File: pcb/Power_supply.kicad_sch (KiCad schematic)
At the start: 32 parts, among them Q1 Si4368DY, SW1 POWER, U1 LTC3872, U2 TLV1117-33

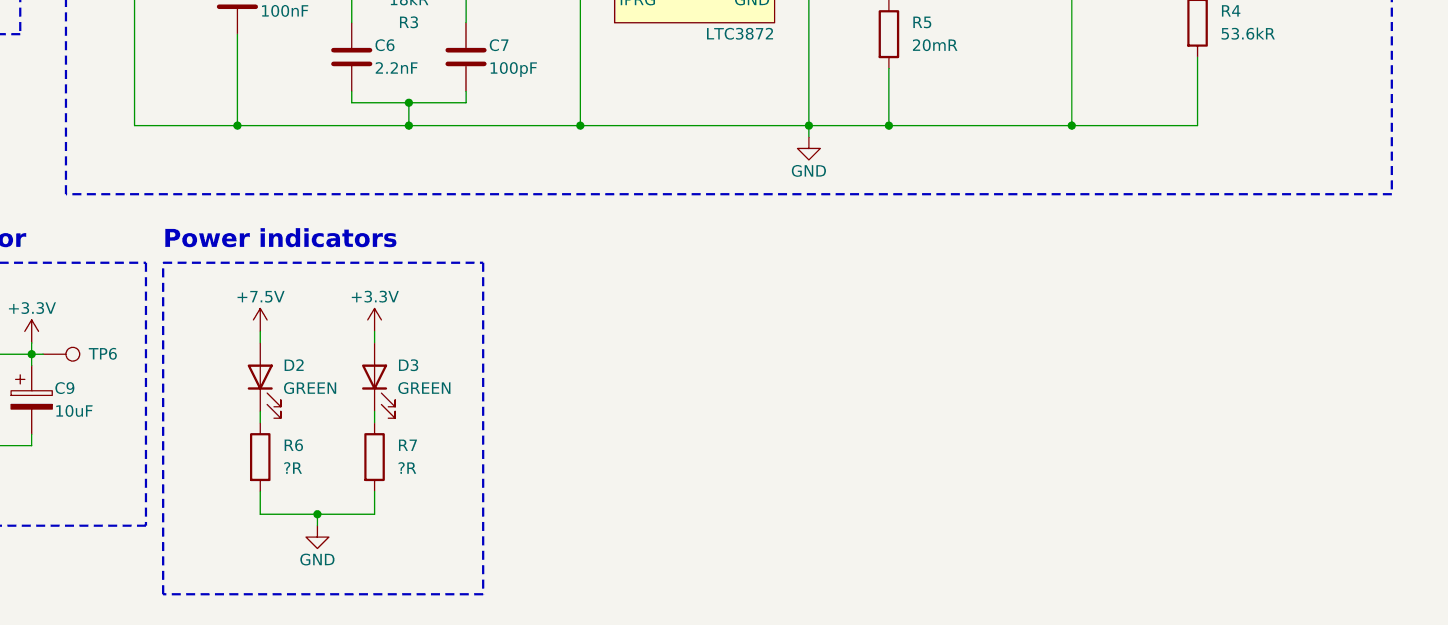
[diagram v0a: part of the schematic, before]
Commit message: [pcb] 4 layer PCB
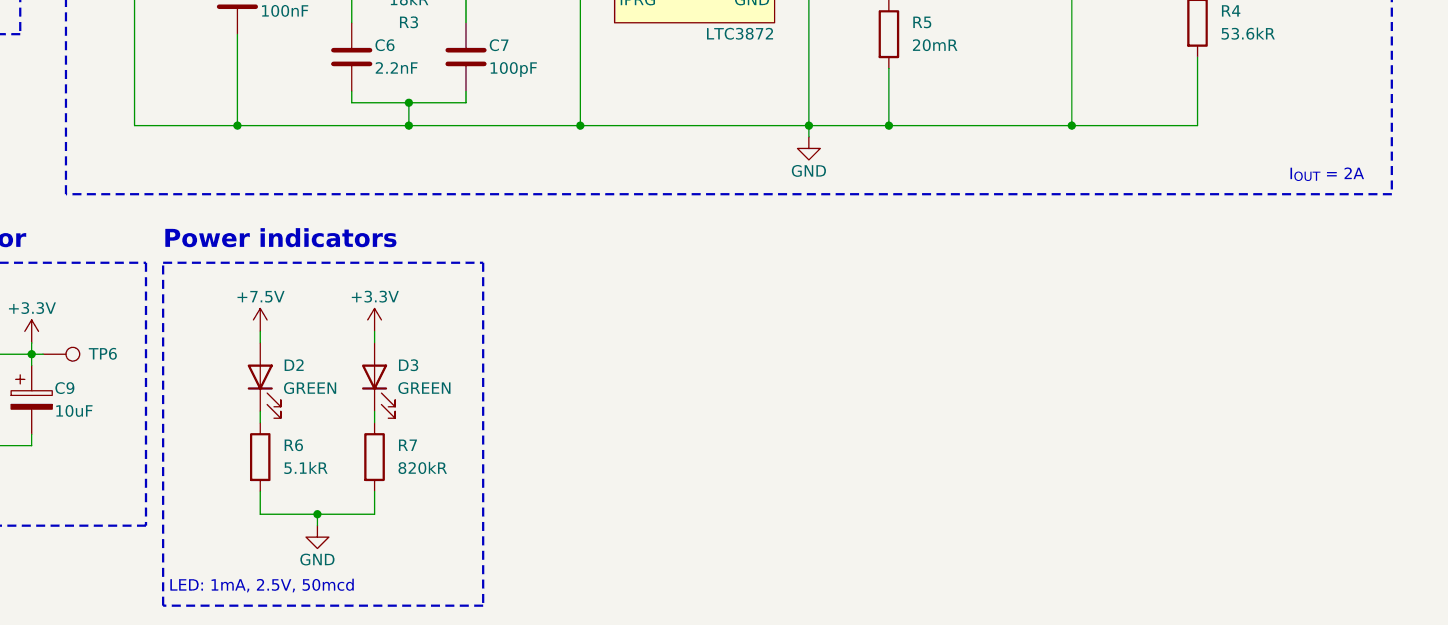
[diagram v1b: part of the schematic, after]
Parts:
- R6: value ?R -> 5.1kR
- R7: value ?R -> 820kR
- U2: footprint Package_TO_SOT_SMD:SOT-223-3_TabPin2 -> Package_TO_SOT_SMD:TO-252-2
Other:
- note added: "I_{OUT} = 2A"
- note added: "LED: 1mA, 2.5V, 50mcd"
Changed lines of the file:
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@@
     (fill (type none))
   )
-  (rectangle (start 71.755 80.01) (end 107.315 116.84)
+  (rectangle (start 71.755 80.01) (end 107.315 118.11)
     (stroke (width 0.25) (type dash))
     (fill (type none))
   )
+  (text "LED: 1mA, 2.5V, 50mcd" (at 72.39 116.84 0)
+    (effects (font (size 1.27 1.27)) (justify left bottom))
+  )
   (text "7.5V boost converter" (at 60.96 21.59 0)
     (effects (font (size 2 2) (thickness 0.4) bold) (justify left bottom))
@@
   (text "3.3V voltage regulator\n" (at 21.59 78.74 0)
     (effects (font (size 2 2) (thickness 0.4) bold) (justify left bottom))
+  )
+  (text "I_{OUT} = 2A" (at 196.85 71.12 0)
+    (effects (font (size 1.27 1.27)) (justify left bottom))
   )
   (symbol (lib_id "Autko:LTC3872") (at 130.81 46.99 0) (unit 1)
@@
       (effects (font (size 1.27 1.27)) (justify left))
     )
-    (property "Value" "?R" (at 97.79 102.87 0)
+    (property "Value" "820kR" (at 97.79 102.87 0)
       (effects (font (size 1.27 1.27)) (justify left))
     )
@@
       (effects (font (size 1.27 1.27)) (justify left))
     )
-    (property "Value" "?R" (at 85.09 102.87 0)
+    (property "Value" "5.1kR" (at 85.09 102.87 0)
       (effects (font (size 1.27 1.27)) (justify left))
     )
@@
       (effects (font (size 1.27 1.27)))
     )
-    (property "Footprint" "Package_TO_SOT_SMD:SOT-223-3_TabPin2" (at 45.72 90.17 0)
-      (effects (font (size 1.27 1.27)) hide)
-    )
+    (property "Footprint" "Package_TO_SOT_SMD:TO-252-2" (at 45.72 90.17 0)
+      (effects (font (size 1.27 1.27)) hide)
+    )

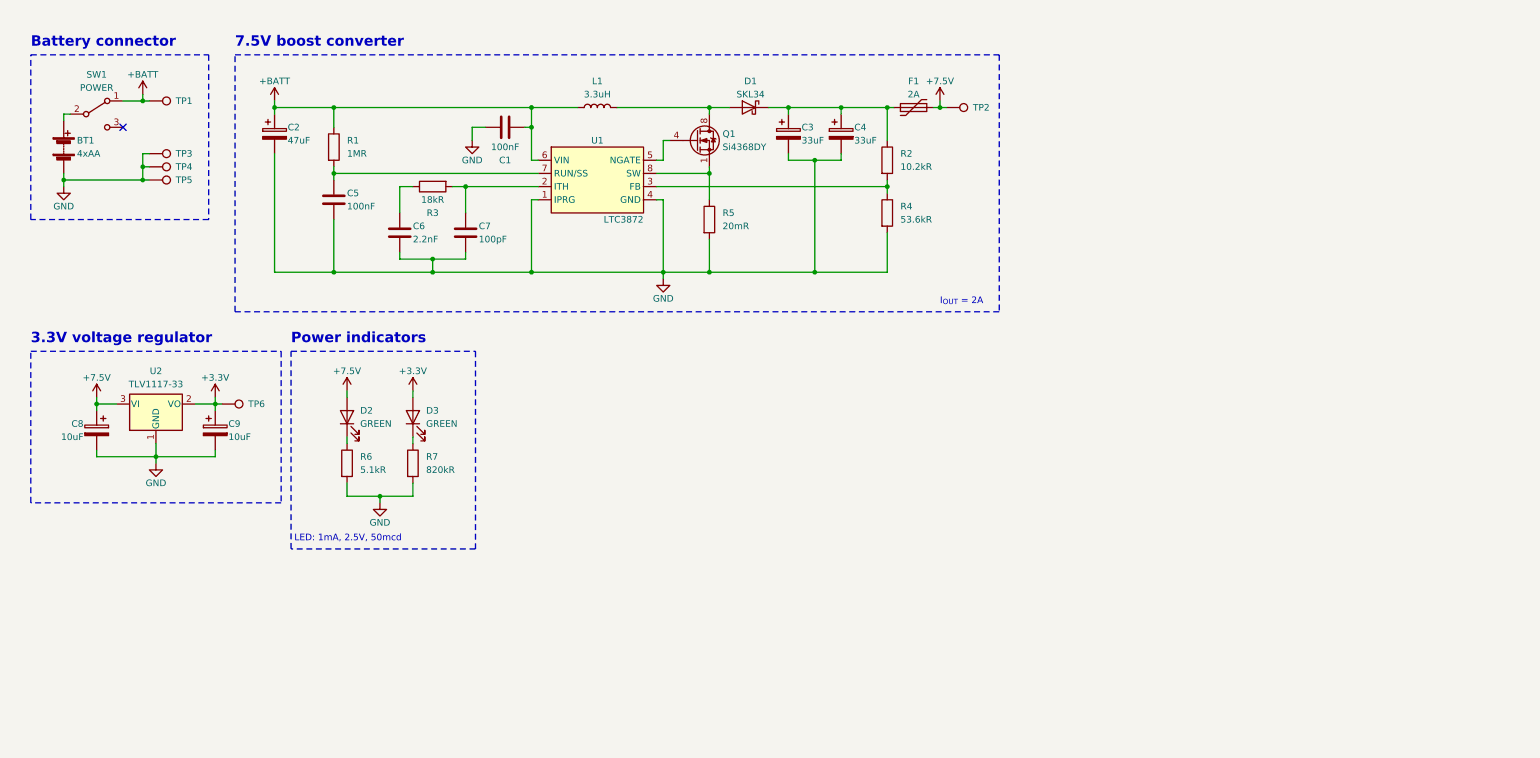
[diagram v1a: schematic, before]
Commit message: [pcb] More final touches, UART test ponts added.
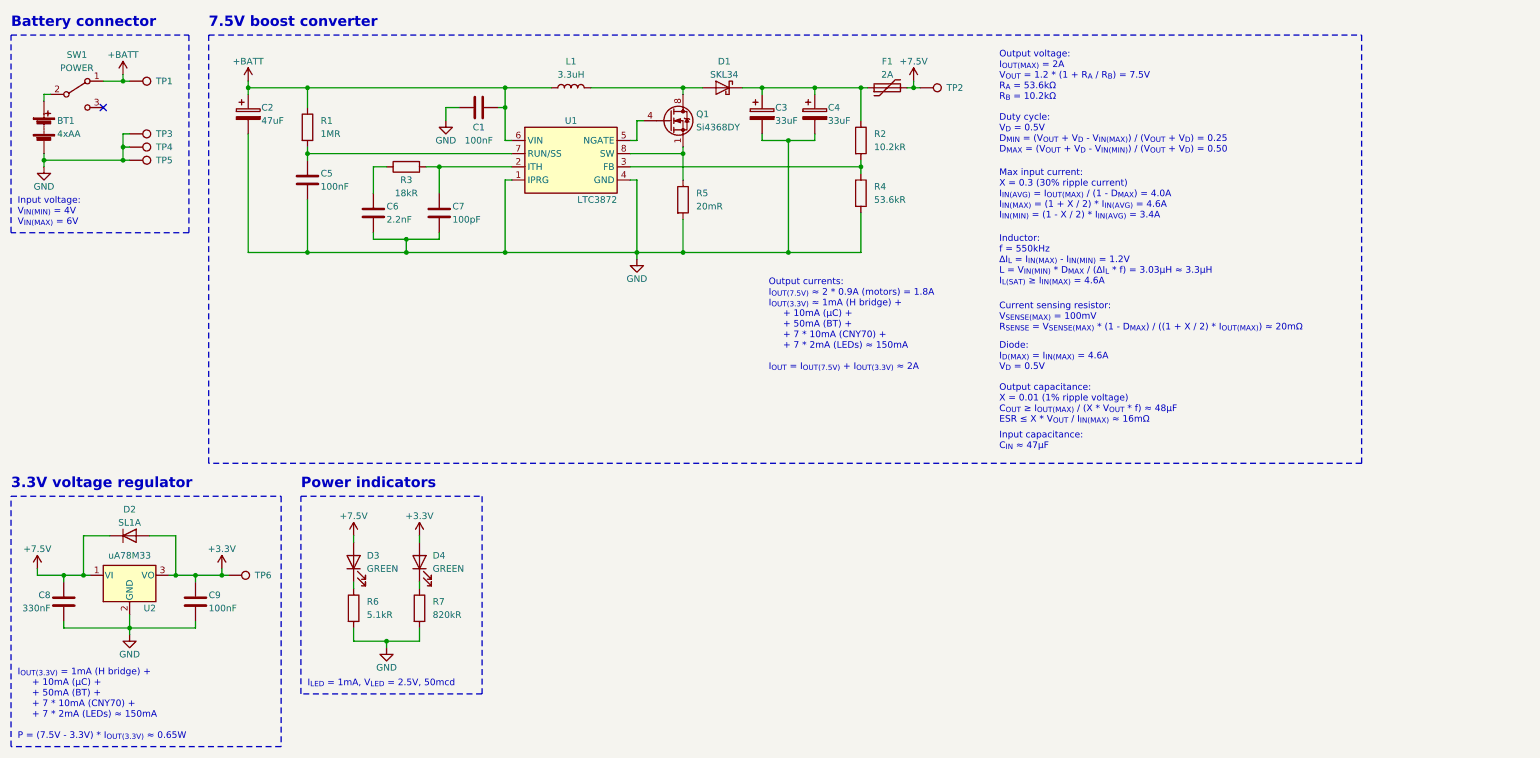
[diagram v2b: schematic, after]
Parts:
- removed C8, C9: 10uF, Capacitor_Tantalum_SMD:CP_EIA-3216-18_Kemet-A, symbol Device:C_Polarized
- removed U2: TLV1117-33, Package_TO_SOT_SMD:TO-252-2, symbol Regulator_Linear:TLV1117-33
- added C8: 330nF, Capacitor_SMD:C_0805_2012Metric, symbol Device:C
- added C9: 100nF, Capacitor_SMD:C_0805_2012Metric, symbol Device:C
- added D2: SL1A, Diode_SMD:D_SOD-123F, symbol Device:D
- added U2: uA78M33, Package_TO_SOT_SMD:SOT-223-3_TabPin2, symbol Autko:uA78M33
- renumbered D2 to D3, D3 to D4
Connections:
- net +3.3V: now also C9.1, D2.2 (A), U2.3 (VO)
- net +7.5V: now also C8.1, D2.1 (K), U2.1 (VI)
- net GND: now also C8.2, C9.2, U2.2 (GND)
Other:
- note added: "Current sensing resistor: V_{SENSE(MAX)} = 100mV R_{SENSE} = V_{SENSE(MAX)} * (1 - D_{MAX}) / ((1 + X / 2) * I_{OUT(MAX)}) ≈ 20mΩ"
- note added: "Diode: I_{D(MAX)} = I_{IN(MAX)} = 4.6A V_{D} = 0.5V"
- note added: "Duty cycle: V_{D} = 0.5V D_{MIN} = (V_{OUT} + V_{D} - V_{IN(MAX)}) / (V_{OUT} + V_{D}) = 0.25 D_{MAX} = (V_{OUT} + V_{D} - V_{IN(MIN)}) / (V_{OUT} + V_{D}) = 0.50"
- note added: "I_{LED} = 1mA, V_{LED} = 2.5V, 50mcd"
- note added: "I_{OUT(3.3V)} = 1mA (H bridge) + + 10mA (µC) + + 50mA (BT) + + 7 * 10mA (CNY70) + + 7 * 2mA (LEDs) ≈ 150mA P = (7.5V - 3.3V) * I_{OUT(3.3V)} ≈ 0.65W"
- note added: "Inductor: f = 550kHz ∆I_{L} = I_{IN(MAX)} - I_{IN(MIN)} = 1.2V L = V_{IN(MIN)} * D_{MAX} / (∆I_{L} * f) = 3.03μH ≈ 3.3μH I_{L(SAT)} ≥ I_{IN(MAX)} = 4.6A"
- note added: "Input capacitance: C_{IN} ≈ 47μF"
- note added: "Input voltage: V_{IN(MIN)} = 4V V_{IN(MAX)} = 6V"
- note added: "Max input current: X = 0.3 (30% ripple current) I_{IN(AVG)} = I_{OUT(MAX)} / (1 - D_{MAX}) = 4.0A I_{IN(MAX)} = (1 + X / 2) * I_{IN(AVG)} = 4.6A I_{IN(MIN)} = (1 - X / 2) * I_{IN(AVG)} = 3.4A"
- note added: "Output capacitance: X = 0.01 (1% ripple voltage) C_{OUT} ≥ I_{OUT(MAX)} / (X * V_{OUT} * f) ≈ 48μF ESR ≤ X * V_{OUT} / I_{IN(MAX)} ≈ 16mΩ"
- note added: "Output currents: I_{OUT(7.5V)} ≈ 2 * 0.9A (motors) = 1.8A I_{OUT(3.3V)} ≈ 1mA (H bridge) + + 10mA (µC) + + 50mA (BT) + + 7 * 10mA (CNY70) + + 7 * 2mA (LEDs) ≈ 150mA I_{OUT} = I_{OUT(7.5V)} + I_{OUT(3.3V)} ≈ 2A"
- note added: "Output voltage: I_{OUT(MAX)} = 2A V_{OUT} = 1.2 * (1 + R_{A} / R_{B}) = 7.5V R_{A} = 53.6kΩ R_{B} = 10.2kΩ"
- note removed: "I_{OUT} = 2A"
- note removed: "LED: 1mA, 2.5V, 50mcd"
- moved on the sheet: BT1, C1, C2, C3, C4, C5, C6, C7, D1, D3, D4, F1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

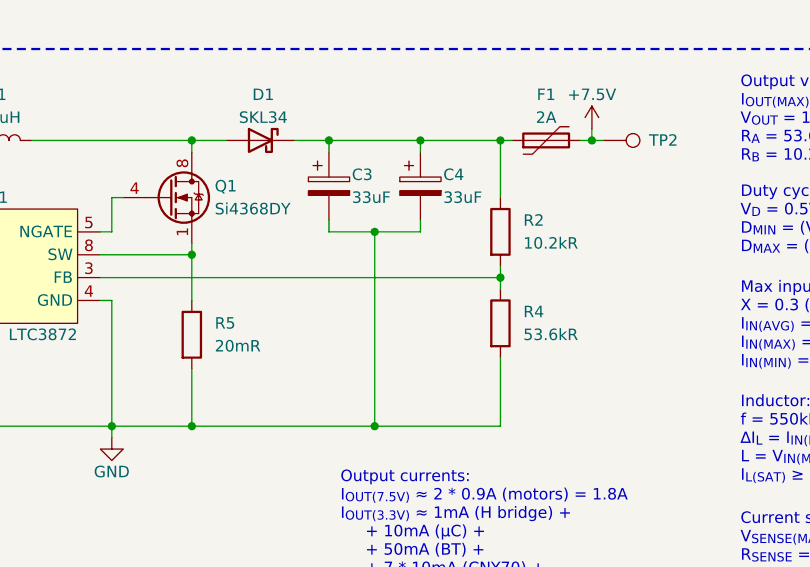
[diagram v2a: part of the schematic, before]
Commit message: [pcb] Mark high-precision resistors
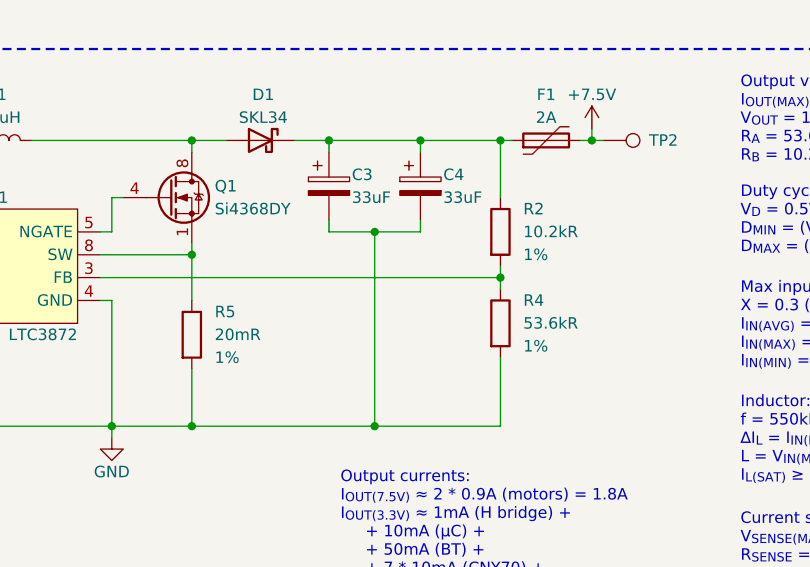
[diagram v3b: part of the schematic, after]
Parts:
- R2, R4, R5: Precision (none) -> 1%
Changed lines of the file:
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@@
   (symbol (lib_id "Device:R") (at 181.61 39.37 0) (unit 1)
     (in_bom yes) (on_board yes) (dnp no)
-    (property "Reference" "R2" (at 184.15 38.1 0)
-      (effects (font (size 1.27 1.27)) (justify left))
-    )
-    (property "Value" "10.2kR" (at 184.15 40.64 0)
+    (property "Reference" "R2" (at 184.15 36.83 0)
+      (effects (font (size 1.27 1.27)) (justify left))
+    )
+    (property "Value" "10.2kR" (at 184.15 39.37 0)
       (effects (font (size 1.27 1.27)) (justify left))
     )
@@
     (property "Datasheet" "~" (at 181.61 39.37 0)
       (effects (font (size 1.27 1.27)) hide)
+    )
+    (property "Precision" "1%" (at 184.15 41.91 0)
+      (effects (font (size 1.27 1.27)) (justify left))
     )
     (pin "1")
@@
   (symbol (lib_id "Device:R") (at 181.61 49.53 0) (unit 1)
     (in_bom yes) (on_board yes) (dnp no)
-    (property "Reference" "R4" (at 184.15 48.26 0)
-      (effects (font (size 1.27 1.27)) (justify left))
-    )
-    (property "Value" "53.6kR" (at 184.15 50.8 0)
+    (property "Reference" "R4" (at 184.15 46.99 0)
+      (effects (font (size 1.27 1.27)) (justify left))
+    )
+    (property "Value" "53.6kR" (at 184.15 49.53 0)
       (effects (font (size 1.27 1.27)) (justify left))
     )
@@
     (property "Datasheet" "~" (at 181.61 49.53 0)
       (effects (font (size 1.27 1.27)) hide)
+    )
+    (property "Precision" "1%" (at 184.15 52.07 0)
+      (effects (font (size 1.27 1.27)) (justify left))
     )
     (pin "1")
@@
   (symbol (lib_id "Device:R") (at 147.32 50.8 0) (unit 1)
     (in_bom yes) (on_board yes) (dnp no)
-    (property "Reference" "R5" (at 149.86 49.53 0)
-      (effects (font (size 1.27 1.27)) (justify left))
-    )
-    (property "Value" "20mR" (at 149.86 52.07 0)
+    (property "Reference" "R5" (at 149.86 48.26 0)
+      (effects (font (size 1.27 1.27)) (justify left))
+    )
+    (property "Value" "20mR" (at 149.86 50.8 0)
       (effects (font (size 1.27 1.27)) (justify left))
     )
@@
       (effects (font (size 1.27 1.27)) hide)
     )
-    (pin "1")
+    (property "Precision" "1%" (at 149.86 53.34 0)
+      (effects (font (size 1.27 1.27)) (justify left))
+    )
+    (pin "1")
